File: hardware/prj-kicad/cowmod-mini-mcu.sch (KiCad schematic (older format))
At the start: 3 parts, among them U1 STM32F750V8

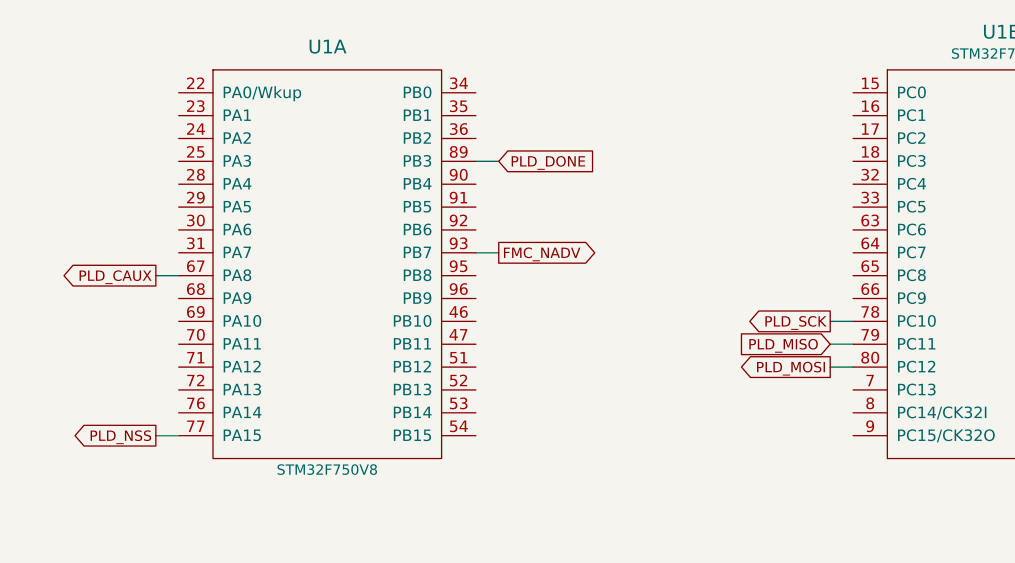
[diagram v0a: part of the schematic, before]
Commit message: = ADD: Insert ethernet network interface
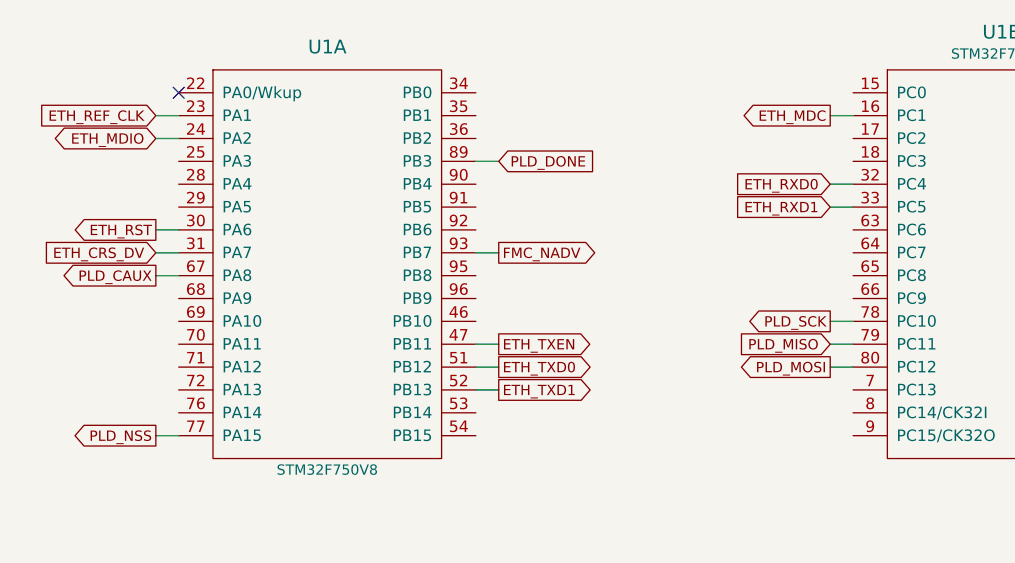
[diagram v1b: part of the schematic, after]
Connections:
- net ETH_MDC: now reaches U1.16 (PC1)
- net ETH_RXD0: now reaches U1.32 (PC4)
- net ETH_RXD1: now reaches U1.33 (PC5)
- net ETH_REF_CLK: now reaches U1.23 (PA1)
- net ETH_MDIO: now reaches U1.24 (PA2)
- net ETH_RST: now reaches U1.30 (PA6)
- net ETH_CRS_DV: now reaches U1.31 (PA7)
- net ETH_TXEN: now reaches U1.47 (PB11)
- net ETH_TXD0: now reaches U1.51 (PB12)
- net ETH_TXD1: now reaches U1.52 (PB13)
- no-connect marks 2 -> 3
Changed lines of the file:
@@
 $Descr A4 11693 8268
 encoding utf-8
-Sheet 3 3
+Sheet 3 4
 Title "Cowmod mini"
 Date ""
@@
 Wire Wire Line
 	2600 3100 2700 3100
+Text GLabel 2600 1700 0    45   Input ~ 0
+ETH_REF_CLK
+Wire Wire Line
+	2600 1700 2700 1700
+Text GLabel 2600 1800 0    45   BiDi ~ 0
+ETH_MDIO
+Wire Wire Line
+	2600 1800 2700 1800
+NoConn ~ 2700 1600
+Text GLabel 5550 1700 0    45   Output ~ 0
+ETH_MDC
+Wire Wire Line
+	5550 1700 5650 1700
+Text GLabel 5550 2000 0    45   Input ~ 0
+ETH_RXD0
+Text GLabel 5550 2100 0    45   Input ~ 0
+ETH_RXD1
+Wire Wire Line
+	5550 2100 5650 2100
+Wire Wire Line
+	5650 2000 5550 2000
+Wire Wire Line
+	4100 2800 4000 2800
+Wire Wire Line
+	4100 2900 4000 2900
+Text GLabel 4100 2800 2    45   Output ~ 0
+ETH_TXD0
+Text GLabel 4100 2900 2    45   Output ~ 0
+ETH_TXD1
+Wire Wire Line
+	4100 2700 4000 2700
+Text GLabel 4100 2700 2    45   Output ~ 0
+ETH_TXEN
+Text GLabel 2600 2200 0    45   Output ~ 0
+ETH_RST
+Wire Wire Line
+	2600 2200 2700 2200
+Text GLabel 2600 2300 0    45   Input ~ 0
+ETH_CRS_DV
+Wire Wire Line
+	2600 2300 2700 2300
 $EndSCHEMATC

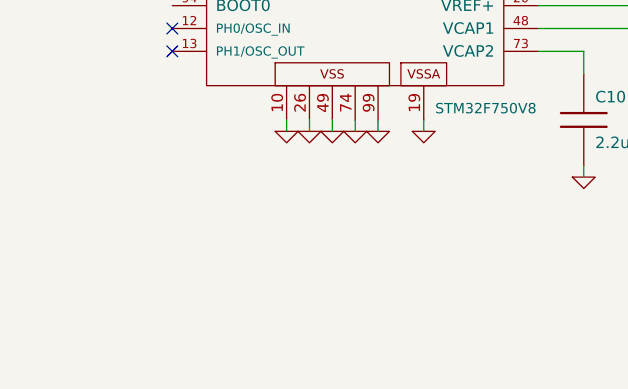
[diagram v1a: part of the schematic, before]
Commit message: = ADD: Insert power supply regulators (3V3 / 1V2 / 2V5)
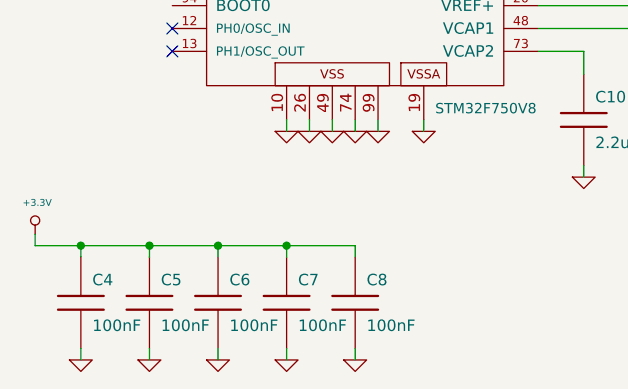
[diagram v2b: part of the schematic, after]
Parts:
- added C4, C5, C6, C7, C8: 100nF, cowmod-mini:SMD0603, symbol cowmod-mini:C
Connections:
- net +3.3V: now also C4.1, C5.1, C6.1, C7.1, C8.1
- net GND: now also C4.2, C5.2, C6.2, C7.2, C8.2
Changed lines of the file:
@@
 $Descr A4 11693 8268
 encoding utf-8
-Sheet 3 4
+Sheet 3 5
 Title "Cowmod mini"
 Date ""
@@
 Wire Wire Line
 	2600 2300 2700 2300
+$Comp
+L cowmod-mini:C C8
+U 1 1 5E3E180B
+P 3350 6400
+F 0 "C8" H 3400 6500 50  0000 L CNN
+F 1 "100nF" H 3400 6300 50  0000 L CNN
+F 2 "cowmod-mini:SMD0603" H 3350 6400 60  0001 C CNN
+F 3 "" H 3350 6400 60  0000 C CNN
+	1    3350 6400
+	1    0    0    -1
+$EndComp
+$Comp
+L cowmod-mini:+3.3V #PWR0197
+U 1 1 5E3E18DA
+P 1950 6100
+F 0 "#PWR0197" H 1950 6060 30  0001 C CNN
+F 1 "+3.3V" H 1959 6238 30  0000 C CNN
+F 2 "" H 1950 6100 60  0000 C CNN
+F 3 "" H 1950 6100 60  0000 C CNN
+	1    1950 6100
+	1    0    0    -1
+$EndComp
+$Comp
+L cowmod-mini:GND #PWR0198
+U 1 1 5E3E191F
+P 3350 6650
+F 0 "#PWR0198" H 3350 6650 30  0001 C CNN
+F 1 "GND" H 3350 6580 30  0001 C CNN
+F 2 "" H 3350 6650 60  0000 C CNN
+F 3 "" H 3350 6650 60  0000 C CNN
+	1    3350 6650
+	1    0    0    -1
+$EndComp
+Wire Wire Line
+	3350 6650 3350 6600
+Wire Wire Line
+	1950 6100 1950 6150
+$Comp
+L cowmod-mini:C C7
+U 1 1 5E3E5747
+P 3050 6400
+F 0 "C7" H 3100 6500 50  0000 L CNN
+F 1 "100nF" H 3100 6300 50  0000 L CNN
+F 2 "cowmod-mini:SMD0603" H 3050 6400 60  0001 C CNN
+F 3 "" H 3050 6400 60  0000 C CNN
+	1    3050 6400
+	1    0    0    -1
+$EndComp
+$Comp
+L cowmod-mini:GND #PWR0199
+U 1 1 5E3E585F
+P 3050 6650
+F 0 "#PWR0199" H 3050 6650 30  0001 C CNN
+F 1 "GND" H 3050 6580 30  0001 C CNN
+F 2 "" H 3050 6650 60  0000 C CNN
+F 3 "" H 3050 6650 60  0000 C CNN
+	1    3050 6650
+	1    0    0    -1
+$EndComp
+Wire Wire Line
+	3050 6650 3050 6600
+Wire Wire Line
+	3050 6150 3350 6150
+Wire Wire Line
+	3350 6150 3350 6200
+Wire Wire Line
+	3050 6150 3050 6200
+$Comp
+L cowmod-mini:C C6
+U 1 1 5E3EB39E
+P 2750 6400
+F 0 "C6" H 2800 6500 50  0000 L CNN
+F 1 "100nF" H 2800 6300 50  0000 L CNN
+F 2 "cowmod-mini:SMD0603" H 2750 6400 60  0001 C CNN
+F 3 "" H 2750 6400 60  0000 C CNN
+	1    2750 6400
+	1    0    0    -1
+$EndComp
+$Comp
+L cowmod-mini:C C5
+U 1 1 5E3EB3E7
+P 2450 6400
+F 0 "C5" H 2500 6500 50  0000 L CNN
+F 1 "100nF" H 2500 6300 50  0000 L CNN
+F 2 "cowmod-mini:SMD0603" H 2450 6400 60  0001 C CNN
+F 3 "" H 2450 6400 60  0000 C CNN
+	1    2450 6400
+	1    0    0    -1
+$EndComp
+Wire Wire Line
+	2450 6150 2450 6200
+Wire Wire Line
+	2450 6150 2750 6150
+Wire Wire Line
+	2750 6150 2750 6200
+Connection ~ 2450 6150
+Wire Wire Line
+	2750 6150 3050 6150
+Connection ~ 2750 6150
+Connection ~ 3050 6150
+Wire Wire Line
+	2750 6650 2750 6600
+Wire Wire Line
+	2450 6650 2450 6600
+$Comp
+L cowmod-mini:GND #PWR0200
+U 1 1 5E3F73D6
+P 2450 6650
+F 0 "#PWR0200" H 2450 6650 30  0001 C CNN
+F 1 "GND" H 2450 6580 30  0001 C CNN
+F 2 "" H 2450 6650 60  0000 C CNN
+F 3 "" H 2450 6650 60  0000 C CNN
+	1    2450 6650
+	1    0    0    -1
+$EndComp
+$Comp
+L cowmod-mini:GND #PWR0201
+U 1 1 5E3F7416
+P 2750 6650
+F 0 "#PWR0201" H 2750 6650 30  0001 C CNN
+F 1 "GND" H 2750 6580 30  0001 C CNN
+F 2 "" H 2750 6650 60  0000 C CNN
+F 3 "" H 2750 6650 60  0000 C CNN
+	1    2750 6650
+	1    0    0    -1
+$EndComp
+$Comp
+L cowmod-mini:C C4
+U 1 1 5E3FA1F7
+P 2150 6400
+F 0 "C4" H 2200 6500 50  0000 L CNN
+F 1 "100nF" H 2200 6300 50  0000 L CNN
+F 2 "cowmod-mini:SMD0603" H 2150 6400 60  0001 C CNN
+F 3 "" H 2150 6400 60  0000 C CNN
+	1    2150 6400
+	1    0    0    -1
+$EndComp
+Wire Wire Line
+	2150 6150 2150 6200
+Wire Wire Line
+	2150 6150 2450 6150
+Wire Wire Line
+	1950 6150 2150 6150
+Connection ~ 2150 6150
+Wire Wire Line
+	2150 6650 2150 6600
+$Comp
+L cowmod-mini:GND #PWR0202
+U 1 1 5E403295
+P 2150 6650
+F 0 "#PWR0202" H 2150 6650 30  0001 C CNN
+F 1 "GND" H 2150 6580 30  0001 C CNN
+F 2 "" H 2150 6650 60  0000 C CNN
+F 3 "" H 2150 6650 60  0000 C CNN
+	1    2150 6650
+	1    0    0    -1
+$EndComp
 $EndSCHEMATC

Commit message: = ADD: Insert an SPI flash for MCU
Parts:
- added U4: M25P16-VME, cowmod-mini:SOIC-8E, symbol cowmod-mini:M25P16-VME
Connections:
- net +3.3V: now also U4.8
- net GND: now also U4.4
- net MEM_IO1: now reaches U1.59 (PD12)
- net MEM_IO1: now also U4.2 (IO1_DO)
- net MEM_IO3: now reaches U1.60 (PD13)
- net MEM_IO3: now also U4.7 (IO3_HOLD)
- net MEM_IO0: now reaches U1.66 (PC9)
- net MEM_IO0: now also U4.5 (IO0_DI)
- net MEM_CLK: now reaches U1.36 (PB2)
- net MEM_CLK: now also U4.6 (CLK)
- net MEM_CS: now reaches U1.92 (PB6)
- net MEM_CS: now also U4.1 (CS)
- net MEM_IO2: now reaches U1.1 (PE2)
- net MEM_IO2: now also U4.3 (IO2_WP)
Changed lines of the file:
@@
 	1    0    0    -1
 $EndComp
+$Comp
+L cowmod-mini:M25P16-VME U4
+U 1 1 5E405974
+P 6950 5150
+F 0 "U4" H 7150 5600 60  0000 C CNN
+F 1 "M25P16-VME" H 7350 4700 60  0000 C CNN
+F 2 "cowmod-mini:SOIC-8E" H 6950 5150 60  0001 C CNN
+F 3 "" H 6950 5150 60  0000 C CNN
+	1    6950 5150
+	1    0    0    -1
+$EndComp
+$Comp
+L cowmod-mini:+3.3V #PWR0203
+U 1 1 5E405B0F
+P 6950 4600
+F 0 "#PWR0203" H 6950 4560 30  0001 C CNN
+F 1 "+3.3V" H 6959 4738 30  0000 C CNN
+F 2 "" H 6950 4600 60  0000 C CNN
+F 3 "" H 6950 4600 60  0000 C CNN
+	1    6950 4600
+	1    0    0    -1
+$EndComp
+Wire Wire Line
+	6950 4600 6950 4700
+Wire Wire Line
+	6950 5650 6950 5600
+$Comp
+L cowmod-mini:GND #PWR0204
+U 1 1 5E40A5C9
+P 6950 5650
+F 0 "#PWR0204" H 6950 5650 30  0001 C CNN
+F 1 "GND" H 6950 5580 30  0001 C CNN
+F 2 "" H 6950 5650 60  0000 C CNN
+F 3 "" H 6950 5650 60  0000 C CNN
+	1    6950 5650
+	1    0    0    -1
+$EndComp
+Text GLabel 4100 2200 2    45   Output ~ 0
+MEM_CS
+Wire Wire Line
+	4100 2200 4000 2200
+Wire Wire Line
+	6350 5000 6450 5000
+Text GLabel 6350 5000 0    45   Input ~ 0
+MEM_CS
+Text GLabel 4100 1800 2    45   Output ~ 0
+MEM_CLK
+Wire Wire Line
+	4100 1800 4000 1800
+Wire Wire Line
+	6350 5300 6450 5300
+Text GLabel 6350 5300 0    45   Input ~ 0
+MEM_CLK
+Text GLabel 7500 4900 2    45   BiDi ~ 0
+MEM_IO0
+Text GLabel 7500 5050 2    45   BiDi ~ 0
+MEM_IO1
+Text GLabel 7500 5250 2    45   BiDi ~ 0
+MEM_IO2
+Text GLabel 7500 5400 2    45   BiDi ~ 0
+MEM_IO3
+Wire Wire Line
+	7500 5400 7400 5400
+Wire Wire Line
+	7400 5250 7500 5250
+Wire Wire Line
+	7500 5050 7400 5050
+Wire Wire Line
+	7400 4900 7500 4900
+Text GLabel 5550 2500 0    45   BiDi ~ 0
+MEM_IO0
+Wire Wire Line
+	5550 2500 5650 2500
+Text GLabel 7050 2900 2    45   BiDi ~ 0
+MEM_IO3
+Wire Wire Line
+	7050 2900 6950 2900
+Text GLabel 7050 2800 2    45   BiDi ~ 0
+MEM_IO1
+Wire Wire Line
+	7050 2800 6950 2800
+Text GLabel 8550 2250 0    45   BiDi ~ 0
+MEM_IO2
+Wire Wire Line
+	8550 2250 8650 2250
 $EndSCHEMATC

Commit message: = UPD: Add missing reset circuit, debug port and simple UART console
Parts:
- added C1: 1uF, cowmod-mini:SMD0603, symbol cowmod-mini:C
- added R1, R2: 10k, cowmod-mini:SMD0603, symbol cowmod-mini:R
- added TP10, TP11: CONN_1, cowmod-mini:TP_PIN, symbol cowmod-mini:CONN_1
- added TP2, TP3, TP4, TP5: CONN_1, cowmod-mini:TP_SMD, symbol cowmod-mini:CONN_1
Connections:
- net labels added: RST, SWD_CLK, SWD_IO
- wire segments 96 -> 115
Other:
- moved on the sheet: C4, C5, C6, C7, C8
